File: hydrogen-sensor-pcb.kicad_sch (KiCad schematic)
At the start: 27 parts, among them J1 Conn_01x02_Socket, J2 Conn_01x04_Pin, J3 Conn_01x02_Socket, SW1 SW_Push, U1 STM32F042F6Px, U2 MQ-8, U3 TCAN1043xDxQ1, U4 LD1117S33TR_SOT223, U5 LD1117S50TR_SOT223, Y1 Crystal_GND24

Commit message: Add power section and move to ESP32
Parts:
- removed C10, C12: 4.7u, symbol Device:C
- removed C11, C9: 1u, symbol Device:C
- removed J3: Conn_01x02_Socket, symbol Connector:Conn_01x02_Socket
- removed U3: TCAN1043xDxQ1, Package_SO:SOIC-14_3.9x8.7mm_P1.27mm, symbol Interface_CAN_LIN:TCAN1043xDxQ1
- removed U4: LD1117S33TR_SOT223, Package_TO_SOT_SMD:SOT-223-3_TabPin2, symbol Regulator_Linear:LD1117S33TR_SOT223
- removed U5: LD1117S50TR_SOT223, Package_TO_SOT_SMD:SOT-223-3_TabPin2, symbol Regulator_Linear:LD1117S50TR_SOT223
- added C27, C28, C29, C30, C31, C32, C33, C34: C, symbol Device:C
- added C35: 1u, symbol Device:C
- added D2, D3, D4: LED, symbol Device:LED
- added D5: SP0502BAJT, Package_TO_SOT_SMD:SOT-323_SC-70, symbol Power_Protection:SP0502BAJT
- added J4: Conn_01x02_Pin, symbol Connector:Conn_01x02_Pin
- added L3: L, symbol Device:L
- added R17, R18: 60, symbol Device:R
- added R19: 499, symbol Device:R
- added R2, R3, R4: 1k, symbol Device:R
- added R5: 10k, symbol Device:R
- added U3: SN65HVD232, Package_SO:SOIC-8_3.9x4.9mm_P1.27mm, symbol Interface_CAN_LIN:SN65HVD232
- added U6: ESP32-S3, Package_DFN_QFN:QFN-56-1EP_7x7mm_P0.4mm_EP5.6x5.6mm, symbol PCM_Espressif:ESP32-S3
- FB1: value 120R -> 120R@100 MHz
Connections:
- net +3.3V: now also C8.1, D4.2 (A), U3.3 (VCC)
- net +5V: no longer C8.1
- net CANH: now also D5.1 (K), R18.1, U3.7 (CANH)
- net CANL: now also D5.2 (K), R17.2, U3.6 (CANL)
- net CAN_RX: now also U3.1 (D)
- net CAN_TX: now also U3.4 (R)
- net GND: now also C27.2, C29.2, C30.2, C31.2, C32.2, C33.2, C34.2, D5.3 (A), J4.2 (Pin_2), R2.2, R3.2, R4.2, R5.2, U3.2 (GND)
- net OSC_A: no longer C4.1, Y1.1
- net OSC_B: no longer C5.1, Y1.3
- net LED_CAN_STATUS: now reaches U1.1 (PB8)
- net LED_CAN_STATUS: now also D3.2 (A)
- net LED_MCU_STATUS: now reaches U1.14 (PB1)
- net LED_MCU_STATUS: now also D2.2 (A)
- new net: C30.1, C32.1, C33.1, L3.1
- new net: R19.1, U6.49 (U0TXD/PROG/GPIO43)
- new net: U6.55 (VDDA), U6.56 (VDDA)
- new net: C27.1, R17.1, R18.2
- new net: D3.1 (K), R2.1
- new net: D4.1 (K), R4.1
- new net: C31.1, L3.2
- new net: D2.1 (K), R3.1
- new net Power /Vin: J4.1 (Pin_1)
- new net VDD3P3: U6.2 (VDD3P3), U6.3 (VDD3P3)
- new net XTAL_N: C4.1, U6.53 (XTAL_N), Y1.1
- new net XTAL_P: C5.1, U6.54 (XTAL_P), Y1.3
- no-connect marks 12 -> 5
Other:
- added sheet Power  (hydrogen-sensor-power-pcb.kicad_sch)
- note added: "C_load - C_stray x 2"
- note added: "I_{VDD_max}: 120 mA P_{max}: 265 mW"
- note added: "I_{max}: 250 mA P_{max}: 800 mW"
- note added: "JTAG debug port"
- note added: "Signal diodes"
- note added: "TODO: ESP32 vs STM32 ESP32 SoC vs module Check crystal osc values Add VDD pins' filters USB C? JTAG+UART Update component numeration Annotate document"
- note added: "TODO: We may use 4 pin connector with CAN"
- note added: "Termination node (resistors and capacitor) may be omitted during assembly if not required."
- note removed: "LDO 3.3 V"
- note removed: "LDO 5 V"
- note removed: "Power supply connector"
- note removed: "SWD debug port"
- note removed: "TODO: LED (Status PB1, CAN PB8) CAN termination resistor & jumper Check crystal osc values Check viability of used IC (cost, voltage, requriements) Check current MQ-8 sensor current requirements Check if CAN transceiver require more pins connected Annotate document"
- moved on the sheet: C1, C13, C14, C15, C2, C3, C4, C5, C6, C7, FB1, J1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

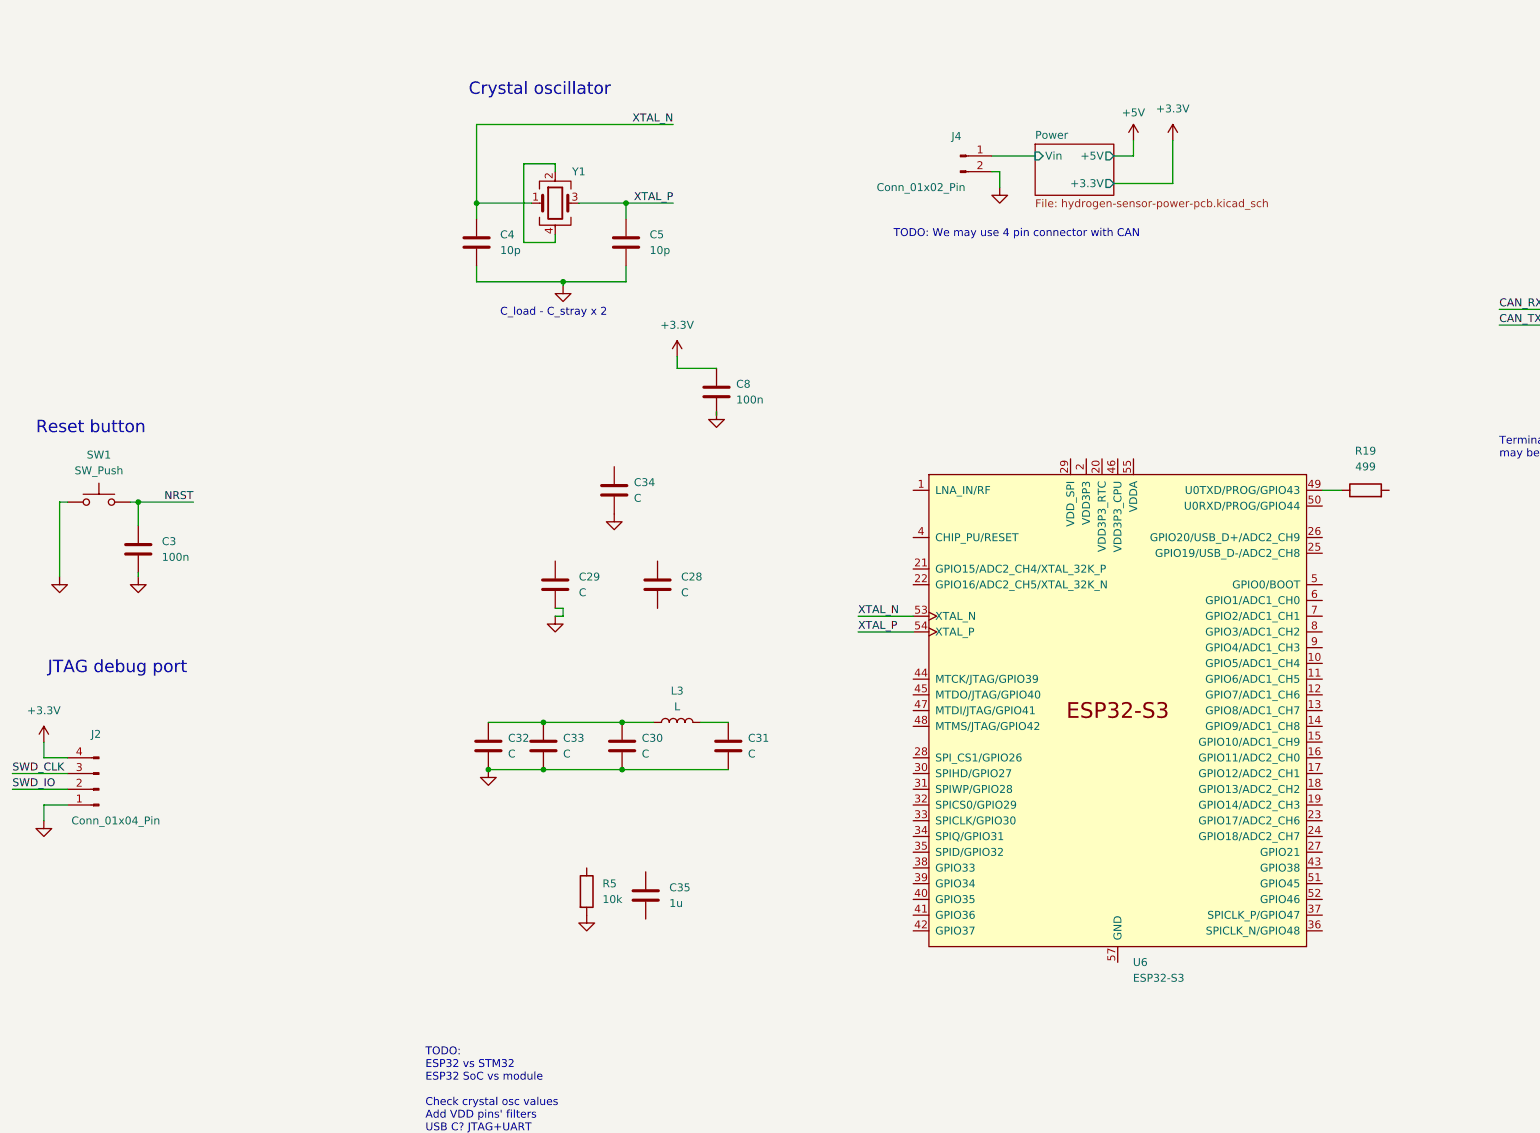
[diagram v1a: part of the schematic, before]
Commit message: Finish Vcc configuration and add USB-C
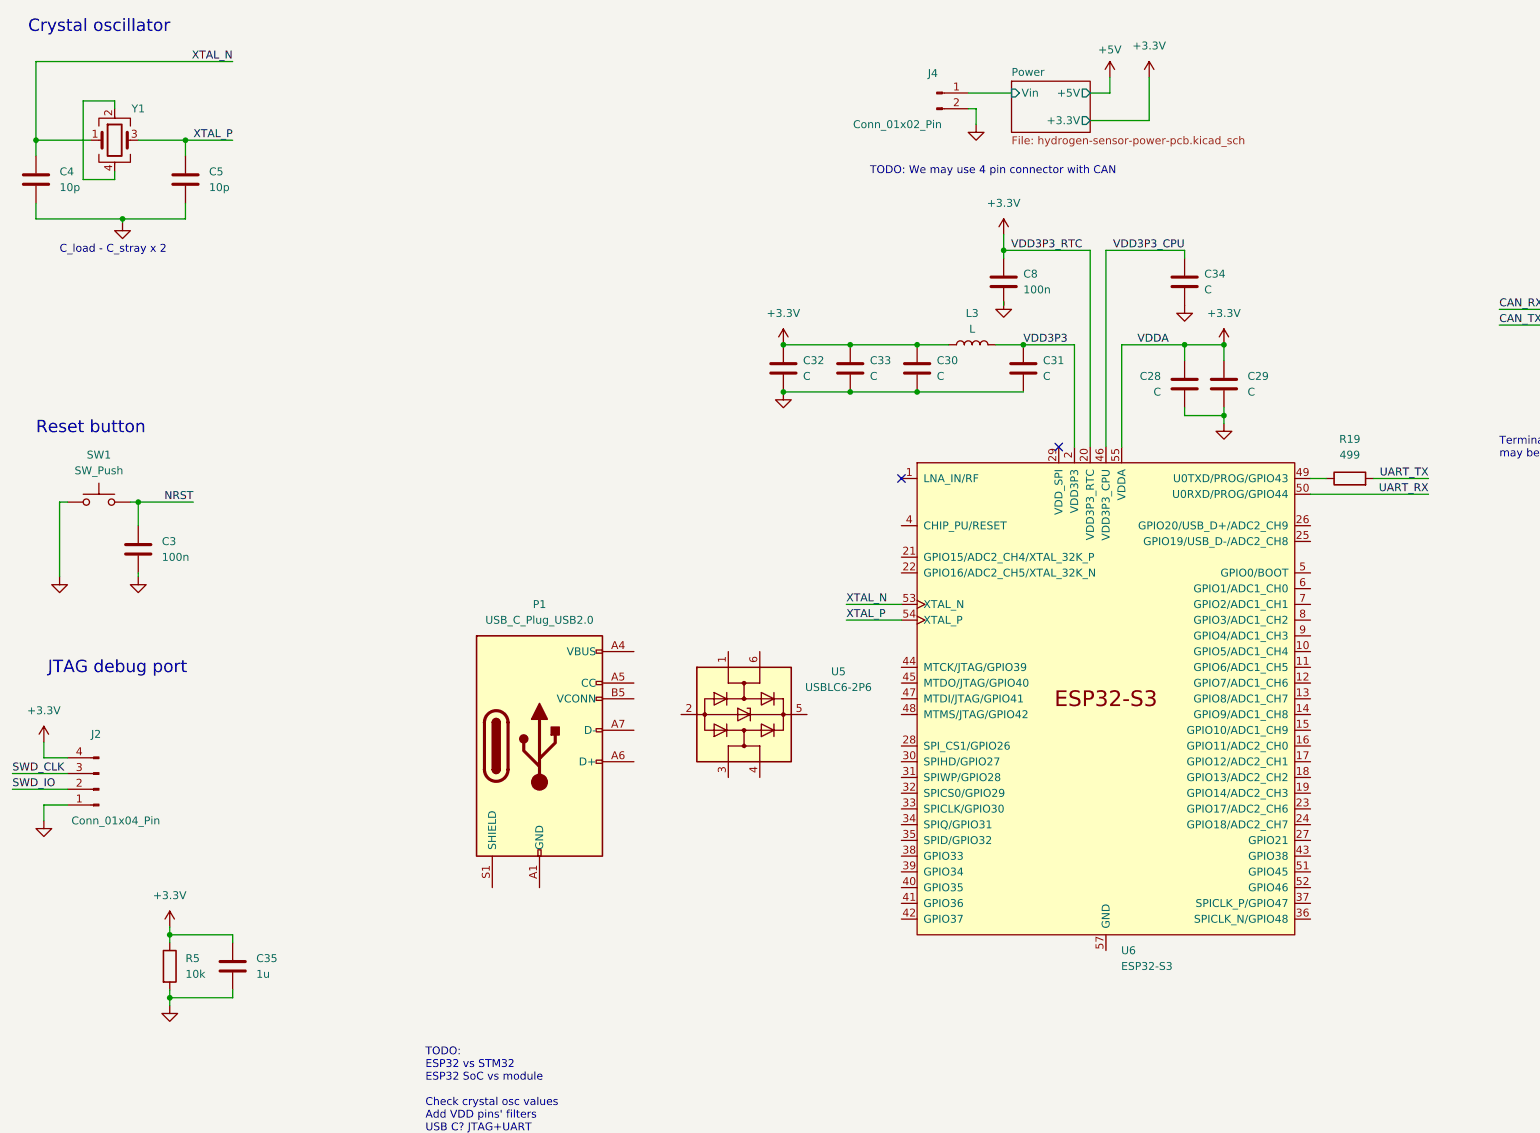
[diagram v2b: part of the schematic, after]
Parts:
- added P1: USB_C_Plug_USB2.0, symbol Connector:USB_C_Plug_USB2.0
- added U5: USBLC6-2P6, Package_TO_SOT_SMD:SOT-666, symbol Power_Protection:USBLC6-2P6
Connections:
- net +3.3V: now also C28.1, C29.1, C30.1, C32.1, C33.1, C35.1, L3.1, R5.1, U6.20 (VDD3P3_RTC), U6.55 (VDDA), U6.56 (VDDA)
- net GND: now also C28.2, C35.2
- net VDD3P3: now also C31.1, L3.2
- net VDD3P3_CPU: now reaches U6.46 (VDD3P3_CPU)
- net VDD3P3_CPU: now also C34.1
- net UART_RX: now reaches U6.50 (U0RXD/PROG/GPIO44)
- net UART_TX: now reaches R19.2
- new net: P1.A1 (GND), P1.A12 (GND), P1.B1 (GND), P1.B12 (GND)
- new net: P1.A4 (VBUS), P1.A9 (VBUS), P1.B4 (VBUS), P1.B9 (VBUS)
- no-connect marks 5 -> 7
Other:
- moved on the sheet: C28, C29, C30, C31, C32, C33, C34, C35, C4, C5, C8, J4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

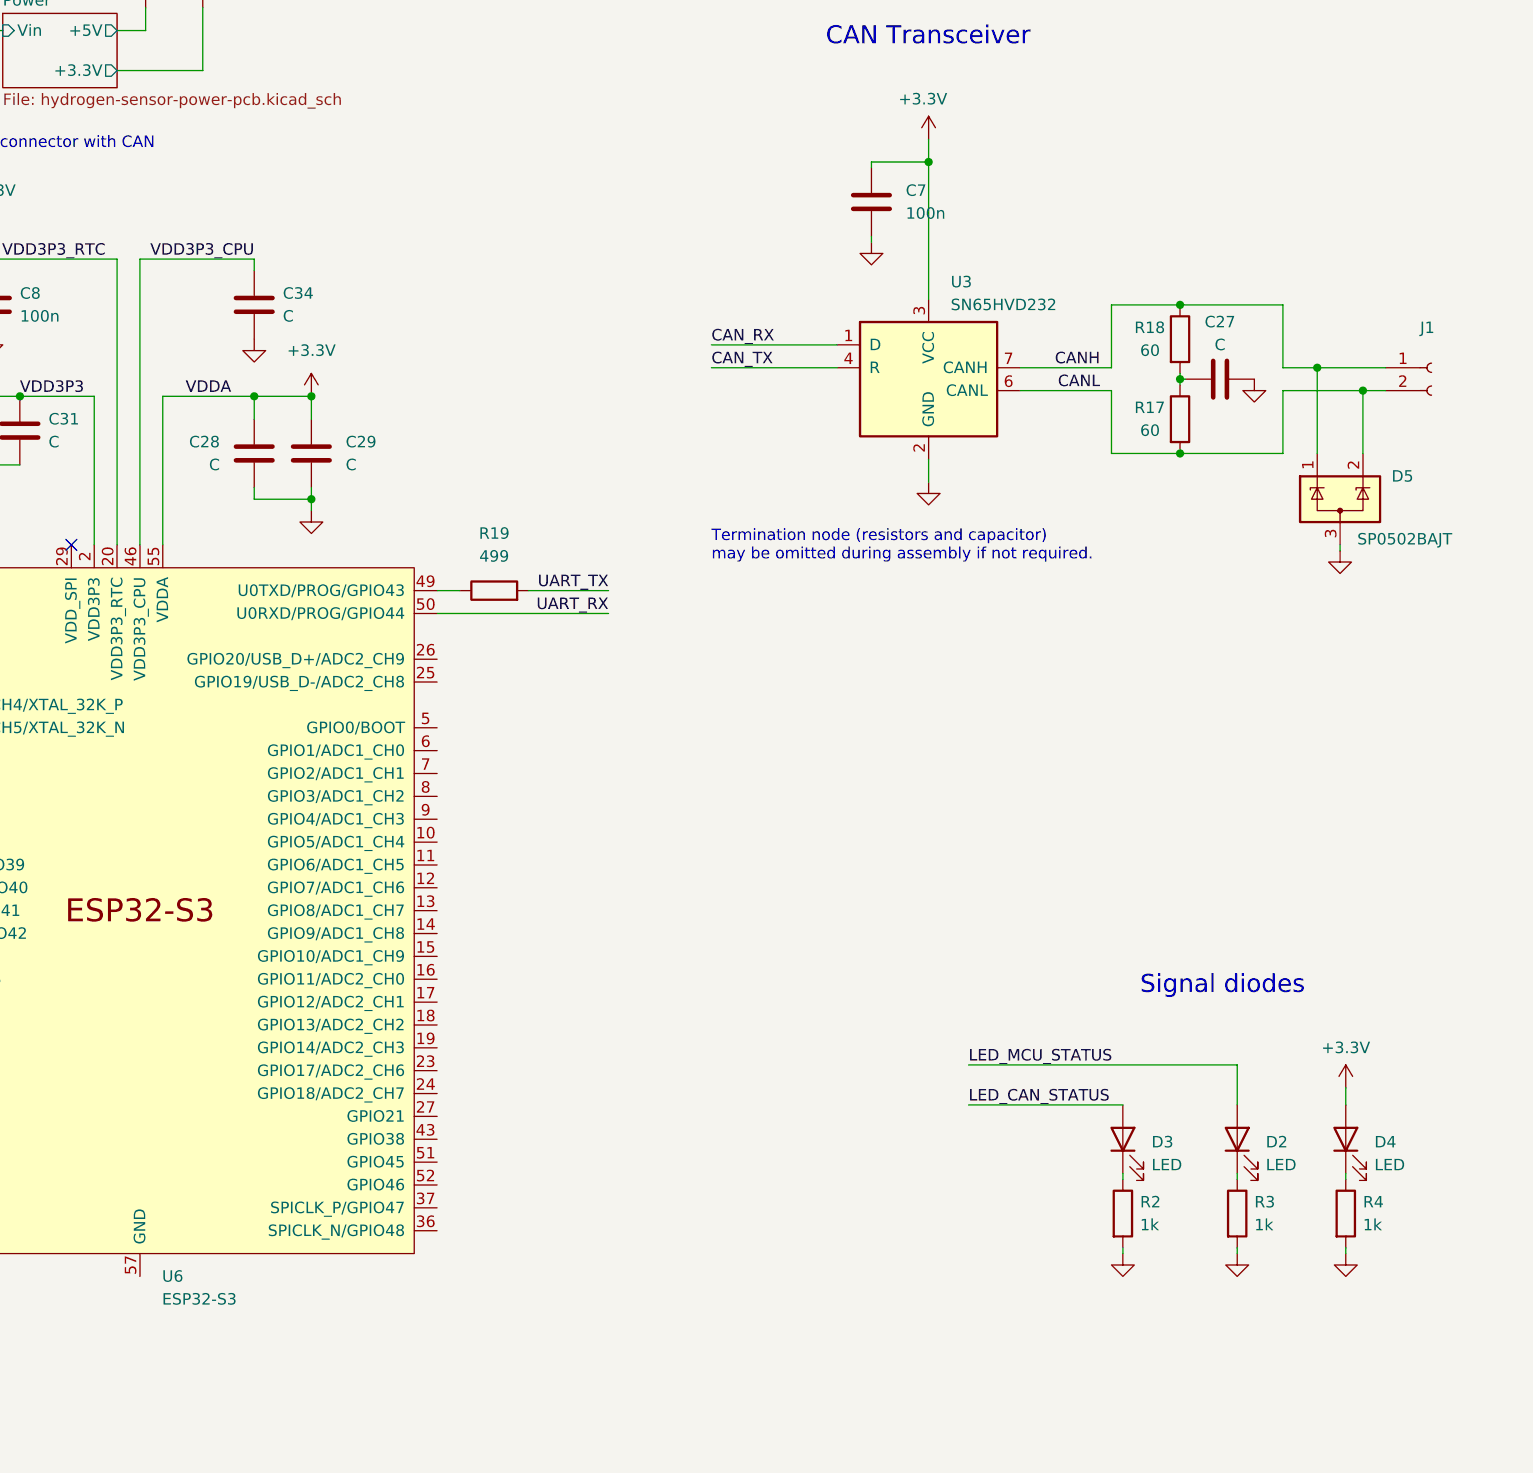
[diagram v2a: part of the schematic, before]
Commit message: Change placement of CAN filter
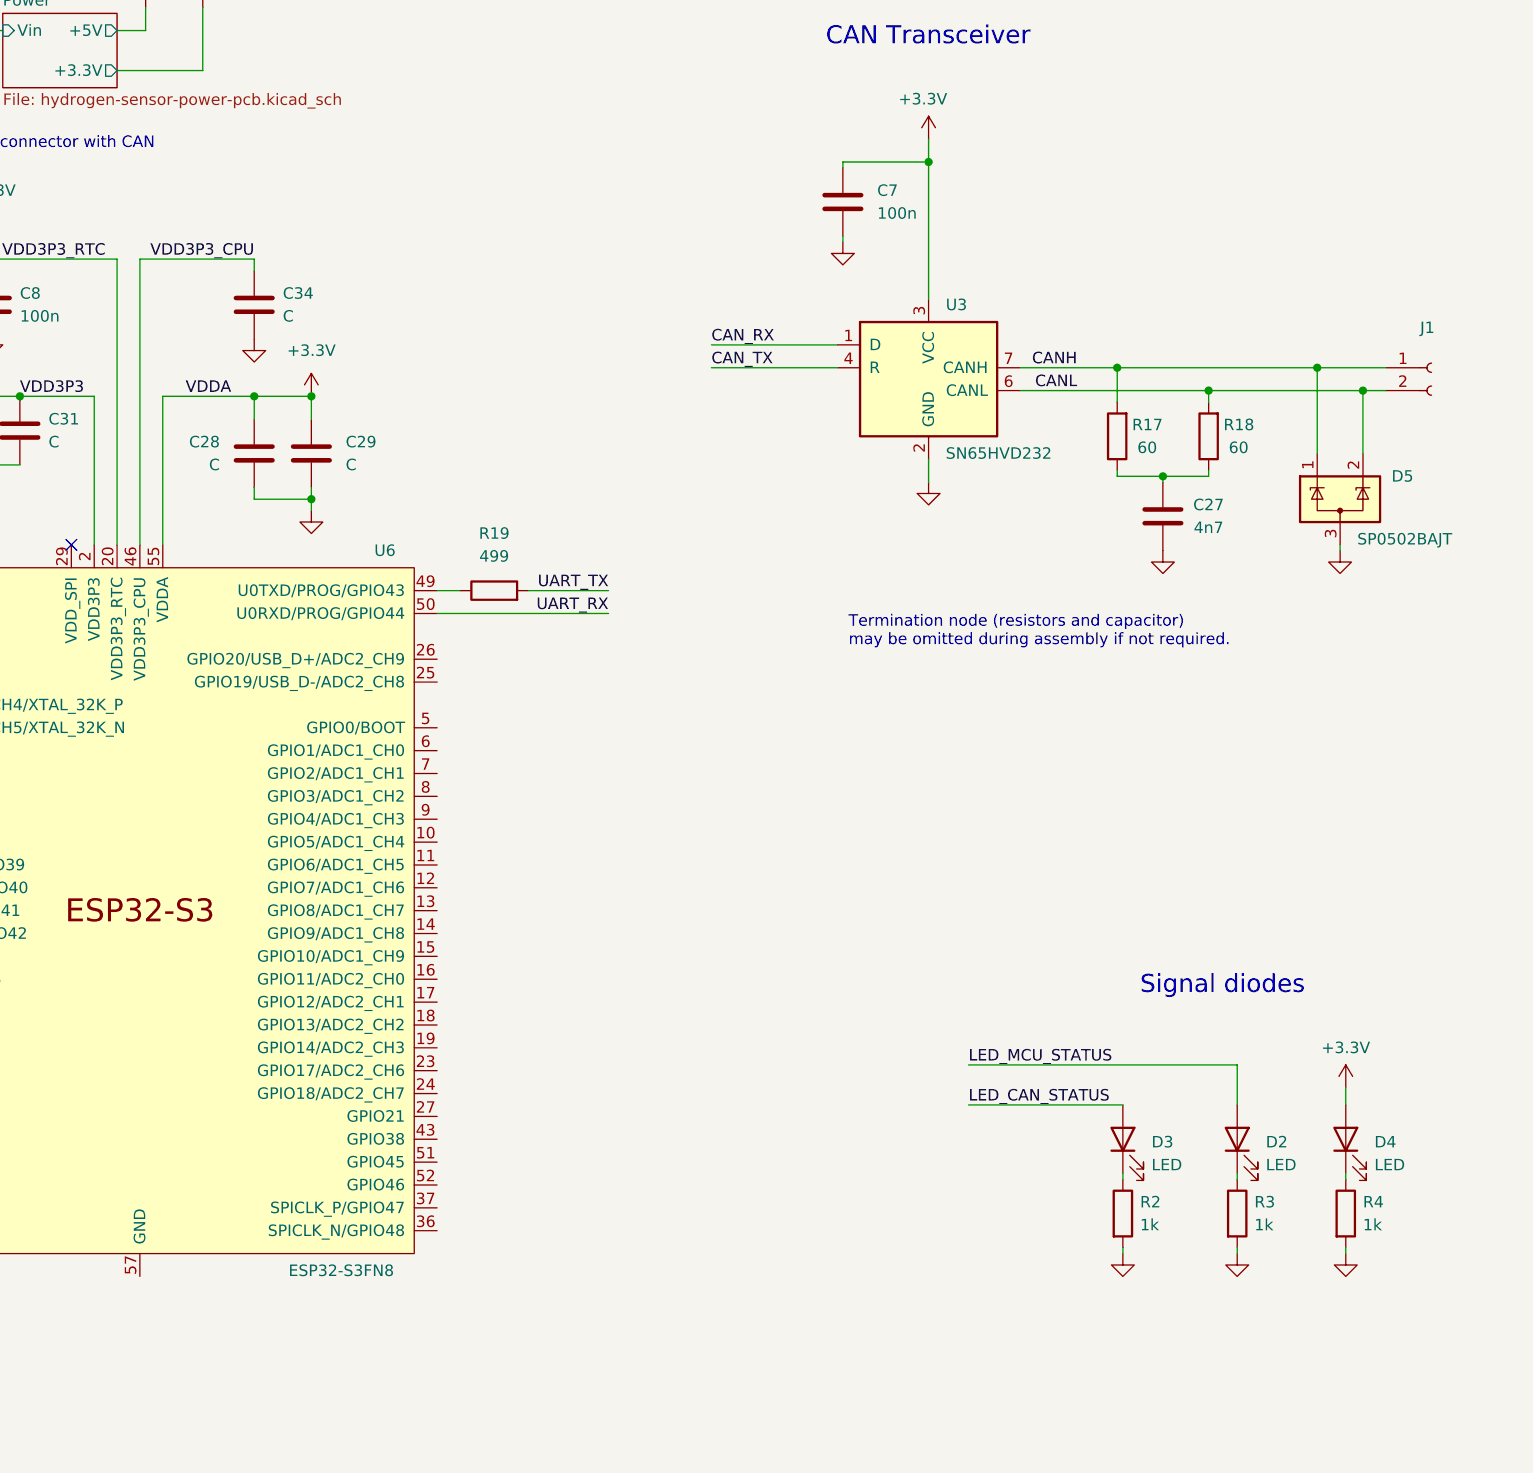
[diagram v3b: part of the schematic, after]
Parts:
- C27: value C -> 4n7
- U6: value ESP32-S3 -> ESP32-S3FN8
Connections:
- net CANH: now also R17.2; no longer R18.1
- net CANL: now also R18.2; no longer R17.2
- net at C27.1, R17.1: now also R18.1; no longer R18.2
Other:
- moved on the sheet: C27, C7, R17, R18
